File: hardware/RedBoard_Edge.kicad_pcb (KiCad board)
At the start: 2 copper layers, 71 parts, among them J1 CONN_025MM, J17 QWIIC_CONNECTORJS-1MM, J2 CONN_03X2SMT, J20 POWER_JACKSMD, J4 USB_MICRO-B_FEMALE-SMT, J5 CONN_04, J6 CONN_04, Q1 MOSFET_PCH-SI2309DS, Q2 MOSFET-NCH-BSS138, Q3 MOSFET-NCH-BSS138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

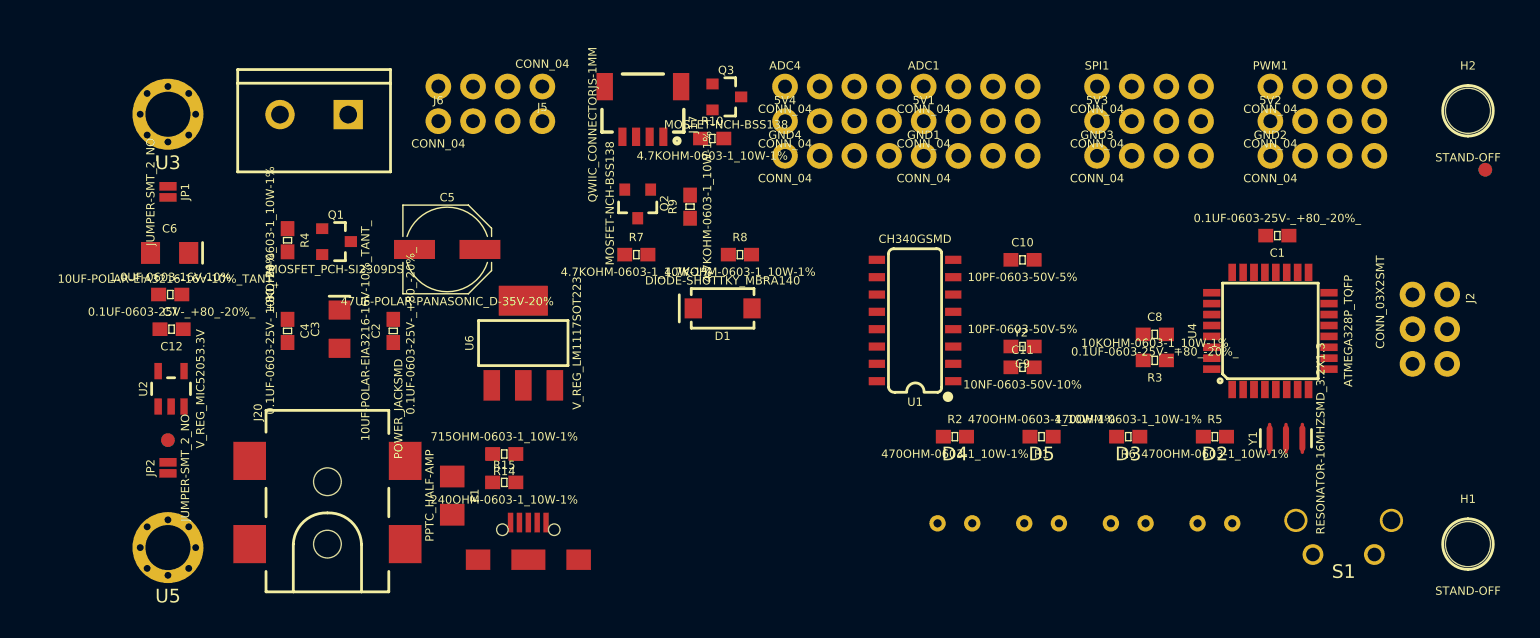
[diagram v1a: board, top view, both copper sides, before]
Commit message: updated toggle switch
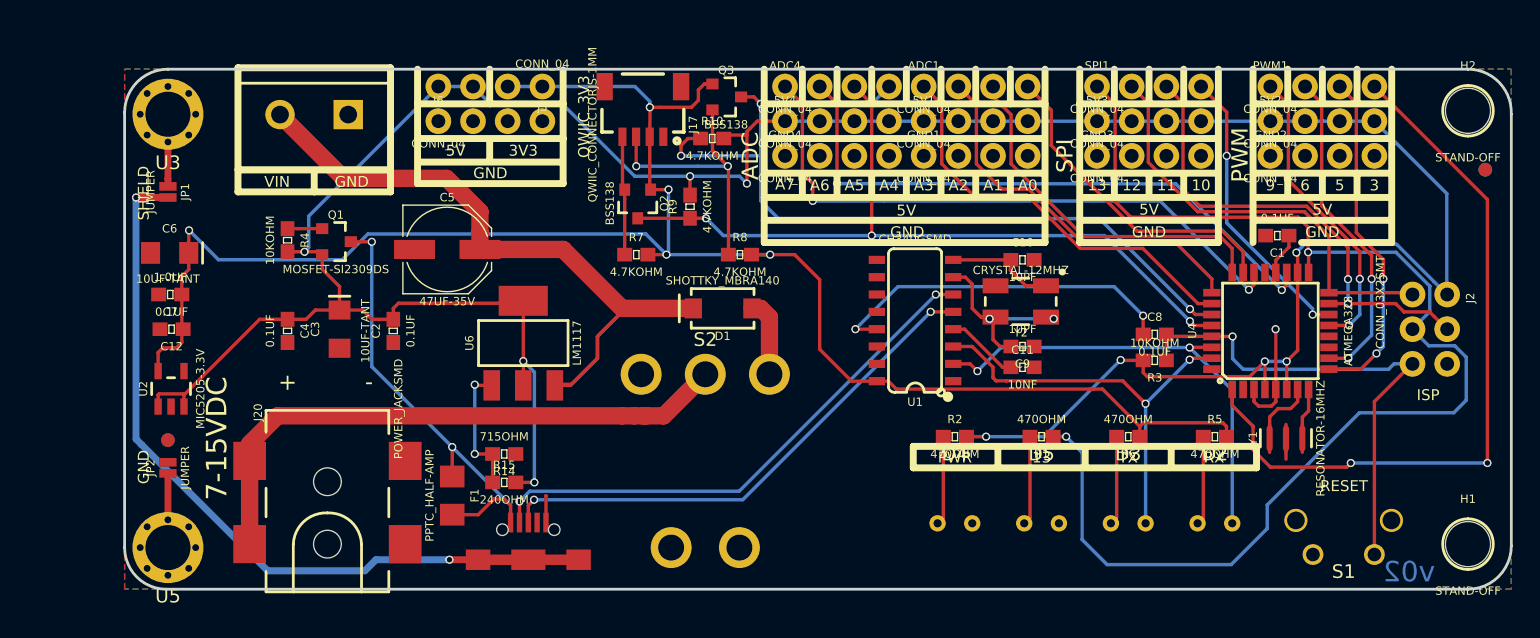
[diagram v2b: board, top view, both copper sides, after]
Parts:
- added S2: SWITCH_TOGGLE, Switches:TOGGLE_SWITCH-102-C3, F.Cu at (143.5, 100.3)
- C1, C12, C2, C4, C8: value 0.1UF-0603-25V-_+80_-20%_ -> 0.1UF
- C10, C9: value 10PF-0603-50V-5% -> 10PF
- C11: value 10NF-0603-50V-10% -> 10NF
- C3, C6: value 10UF-POLAR-EIA3216-16V-10%_TANT_ -> 10UF-TANT
- C5: value 47UF-POLAR-PANASONIC_D-35V-20% -> 47UF-35V
- C7: value 1.0UF-0603-16V-10% -> 1.0UF
- D1: value DIODE-SHOTTKY_MBRA140 -> SHOTTKY_MBRA140
- D2: value SPARKFUN-LED_LED-YELLOW-550 -> LED-YELLOW
- D3: value SPARKFUN-LED_LED-GREEN-550 -> LED-GREEN
- D4: value SPARKFUN-LED_LED-RED-550 -> LED-RED
- D5: value SPARKFUN-LED_LED-YELLOW-550 -> LED-BLUE
- J4: value USB_MICRO-B_FEMALE-SMT -> USB_MICRO-B
- JP1, JP2: value JUMPER-SMT_2_NO -> JUMPER
- Q1: value MOSFET_PCH-SI2309DS -> MOSFET-SI2309DS
- Q2, Q3: value MOSFET-NCH-BSS138 -> BSS138
- R1, R2, R5, R6: value 470OHM-0603-1_10W-1% -> 470OHM
- R10, R7, R8, R9: value 4.7KOHM-0603-1_10W-1% -> 4.7KOHM
- R14: value 715OHM-0603-1_10W-1% -> 715OHM
- R15: value 240OHM-0603-1_10W-1% -> 240OHM
- R3, R4: value 10KOHM-0603-1_10W-1% -> 10KOHM
- S1: value MOMENTARY-SWITCH-SPST-2-PTH-RT-ANGLE -> MOMENTARY-SWITCH
- U2: value V_REG_MIC52053.3V -> MIC5205-3.3V
- U4: value ATMEGA328P_TQFP -> ATMEGA328
- U6: value V_REG_LM1117SOT223 -> LM1117
- Y1: value RESONATOR-16MHZSMD_3.2X1.3 -> RESONATOR-16MHZ
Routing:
- net 5V: track 0.00 -> 218.1 mm, vias 0 -> 10
- net 3.3V: track 0.00 -> 132.3 mm, vias 0 -> 5
- net /SCK: track 0.00 -> 92.7 mm, vias 0 -> 2
- net VIN: track 0.00 -> 67.3 mm
- net /HI_SDA: track 0.00 -> 63.4 mm, vias 0 -> 3
- net /usb_shield: track 0.00 -> 60.5 mm, vias 0 -> 2
- net /HI_SCL: track 0.00 -> 56.8 mm, vias 0 -> 3
- net /PWM3: track 0.00 -> 53.9 mm, vias 0 -> 2
- net /AD7: track 0.00 -> 45.3 mm, vias 0 -> 2
- net /AD6: track 0.00 -> 44.9 mm, vias 0 -> 2
- net Net-(J20-PadVIN0): track 0.00 -> 42.8 mm
- net Net-(J4-PadD-): track 0.00 -> 39.6 mm, vias 0 -> 2
- net Net-(J4-PadD+): track 0.00 -> 38.3 mm, vias 0 -> 2
- net /RESET: track 0.00 -> 37.2 mm, vias 0 -> 1
- net /MOSI: track 0.00 -> 35.4 mm, vias 0 -> 2
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- added copper zone on B.Cu, net GND
- added copper zone on F.Cu, net GND
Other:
- board outline added: 101.6 x 38.1 mm
- board text added: "+"
- board text added: "-"
- board text added: "10"
- board text added: "11"
- board text added: "12"
- board text added: "13"
- board text added: "3"
- board text added: "3V3"
- board text added: "5"
- board text added: "5V"
- board text added: "6"
- board text added: "7-15VDC"
- board text added: "9"
- board text added: "A0"
- board text added: "A1"
- board text added: "A2"
- board text added: "A3"
- board text added: "A4"
- board text added: "A5"
- board text added: "A6"
- board text added: "A7"
- board text added: "ADC"
- board text added: "Designed by: Nick Poole"
- board text added: "GND"
- board text added: "ISP"
- board text added: "PWM"
- board text added: "PWR"
- board text added: "QWIIC"
- board text added: "RESET"
- board text added: "RX"
- board text added: "RedBoard Edge"
- board text added: "Revised by: Andy England"
- board text added: "SHIELD"
- board text added: "SPI"
- board text added: "Standoff O.C."
- board text added: "TX"
- board text added: "VIN"
- board text added: "v02"

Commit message: fixed xtal
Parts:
- Y2: footprint Clocks:CRYSTAL-SMD-5X3.2-4PAD -> Clocks:CRYSTAL-SMD-3.2X2.5MM
- moved Y2 0.13 mm to (166.6, 96.4)
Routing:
- net Net-(C9-Pad2): track 13.3 -> 9.59 mm, vias 2 -> 0

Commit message: checklist changes
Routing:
- net VIN: track 67.3 -> 63.7 mm
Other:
- board text added: "Design by: Nick Poole"
- board text added: "v10"
- board text removed: "v02"
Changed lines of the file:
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@@
     (area 83.030287 71.214 220.880715 144.86)
     (thickness 1.6)
-    (drawings 388)
-    (tracks 555)
+    (drawings 390)
+    (tracks 554)
     (zones 0)
     (modules 72)
@@
   (page A4)
   (title_block
+    (title "RedBoard Edge")
     (comment 1 https://creativecommons.org/licenses/by-sa/4.0/)
     (comment 2 "Released under the Creative Commons Attribution Share-Alike 4.0 License")
@@
       (solder_mask_margin 0.1016))
   )
+  (gr_text "Revised by: Andy England" (at 264.287 189.865) (layer Cmts.User)
+    (effects (font (size 1.5 1.5) (thickness 0.3)))
+  )
+  (gr_text "Design by: Nick Poole" (at 223.266 189.865) (layer Cmts.User)
+    (effects (font (size 1.5 1.5) (thickness 0.3)))
+  )
   (gr_text 3V3 (at 134.62 80.772 90) (layer F.SilkS)
     (effects (font (size 0.8 0.8) (thickness 0.2)))
@@
     (effects (font (size 1.5 1.5) (thickness 0.3)))
   )
-  (gr_text v02 (at 195.072 116.078) (layer B.Cu)
+  (gr_text v10 (at 195.072 116.078) (layer B.Cu)
     (effects (font (size 1.5 1.5) (thickness 0.3)) (justify mirror))
   )
@@
   (segment (start 129.62636 109.5248) (end 130.9878 109.5248) (width 0.25) (layer F.Cu) (net 3))
   (via (at 130.9878 109.5248) (size 0.6) (drill 0.4) (layers F.Cu B.Cu) (net 3))
+  (segment (start 135.6106 100.4316) (end 137.795 98.2472) (width 0.25) (layer F.Cu) (net 4))
+  (segment (start 137.795 97.155) (end 137.414 96.774) (width 0.25) (layer F.Cu) (net 4))
+  (segment (start 137.795 98.2472) (end 137.795 97.155) (width 0.25) (layer F.Cu) (net 4))
   (segment (start 142.50416 96.774) (end 137.414 96.774) (width 1.27) (layer F.Cu) (net 4))
   (segment (start 126.2507 92.456) (end 133.096 92.456) (width 0.25) (layer F.Cu) (net 4))
   (segment (start 133.096 92.456) (end 137.414 96.774) (width 0.25) (layer F.Cu) (net 4))
   (segment (start 137.414 96.774) (end 137.414 97.02546) (width 0.25) (layer F.Cu) (net 4))
-  (segment (start 137.414 97.02546) (end 135.6106 98.82886) (width 0.25) (layer F.Cu) (net 4))
-  (segment (start 135.6106 98.82886) (end 135.6106 100.4316) (width 0.25) (layer F.Cu) (net 4))
+  (segment (start 137.414 96.774) (end 137.414 97.02546) (width 0.25) (layer F.Cu) (net 4))
   (segment (start 135.6106 100.4316) (end 133.6284 102.4138) (width 0.25) (layer F.Cu) (net 4))
   (segment (start 133.6284 102.4138) (end 132.4864 102.4138) (width 0.25) (layer F.Cu) (net 4))
@@
   (segment (start 135.6106 100.4316) (end 133.70814 102.33406) (width 0.25) (layer F.Cu) (net 4))
   (segment (start 133.70814 102.33406) (end 132.461 102.33406) (width 0.25) (layer F.Cu) (net 4))
-  (segment (start 135.6106 98.82886) (end 135.6106 100.4316) (width 0.25) (layer F.Cu) (net 4))
-  (segment (start 137.414 96.774) (end 133.096 92.456) (width 1.27) (layer F.Cu) (net 4))
-  (segment (start 137.414 96.774) (end 137.414 97.02546) (width 0.25) (layer F.Cu) (net 4))
-  (segment (start 137.414 97.02546) (end 135.6106 98.82886) (width 0.25) (layer F.Cu) (net 4))
+  (segment (start 137.414 96.774) (end 133.096 92.456) (width 1.27) (layer F.Cu) (net 4) (status 2))
   (segment (start 139.446 82.042) (end 140.208 82.042) (width 0.25) (layer F.Cu) (net 5))
   (segment (start 143.44396 80.33004) (end 143.002 80.772) (width 0.25) (layer F.Cu) (net 5))
@@
   (segment (start 177.292 80.518) (end 178.509201 81.735201) (width 0.25) (layer F.Cu) (net 31))
   (segment (start 178.509201 81.735201) (end 178.509201 88.047567) (width 0.25) (layer F.Cu) (net 31))
-  (segment (start 195.32346 95.62592) (end 195.45554 95.758) (width 0.25) (layer F.Cu) (net 32))
-  (segment (start 187.40519 89.69139) (end 189.2046 91.4908) (width 0.25) (layer F.Cu) (net 32))
   (segment (start 189.2046 91.4908) (end 189.2046 95.62592) (width 0.25) (layer F.Cu) (net 32))
+  (segment (start 187.40519 89.69139) (end 189.2046 91.4908) (width 0.25) (layer F.Cu) (net 32))
   (segment (start 174.752 80.518) (end 175.969201 81.735201) (width 0.25) (layer F.Cu) (net 32))
   (segment (start 175.969201 81.735201) (end 175.969201 86.076659) (width 0.25) (layer F.Cu) (net 32))
   (segment (start 175.969201 86.076659) (end 179.583932 89.69139) (width 0.25) (layer F.Cu) (net 32))
   (segment (start 179.583932 89.69139) (end 187.40519 89.69139) (width 0.25) (layer F.Cu) (net 32))
+  (segment (start 195.32346 95.62592) (end 195.45554 95.758) (width 0.25) (layer F.Cu) (net 32))
   (segment (start 189.2046 95.62592) (end 195.16852 95.62592) (width 0.25) (layer F.Cu) (net 32))
   (segment (start 195.16852 95.62592) (end 195.3006 95.758) (width 0.25) (layer F.Cu) (net 32))
